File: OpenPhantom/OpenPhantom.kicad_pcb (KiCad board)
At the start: 2 copper layers, 175 x 175 mm, 94 parts, among them J1 Barrel_Jack, J2 Video, J3 Audio, Q1 BC548, Q2 BD136, Q3 BC557, Q4 BC548, SW1 POWER, SW2 RESET, U1 UM6116 VRAM, U10 74HC368, U11 74HC368, U2 UM6116 WRAM, U3 74HC04, U4 UA6547_CPU, U5 4013, U6 UA6548_PPU, U7 74HC139, U8 74LS373, U9 LM7805, Y1 21.453366 MHz

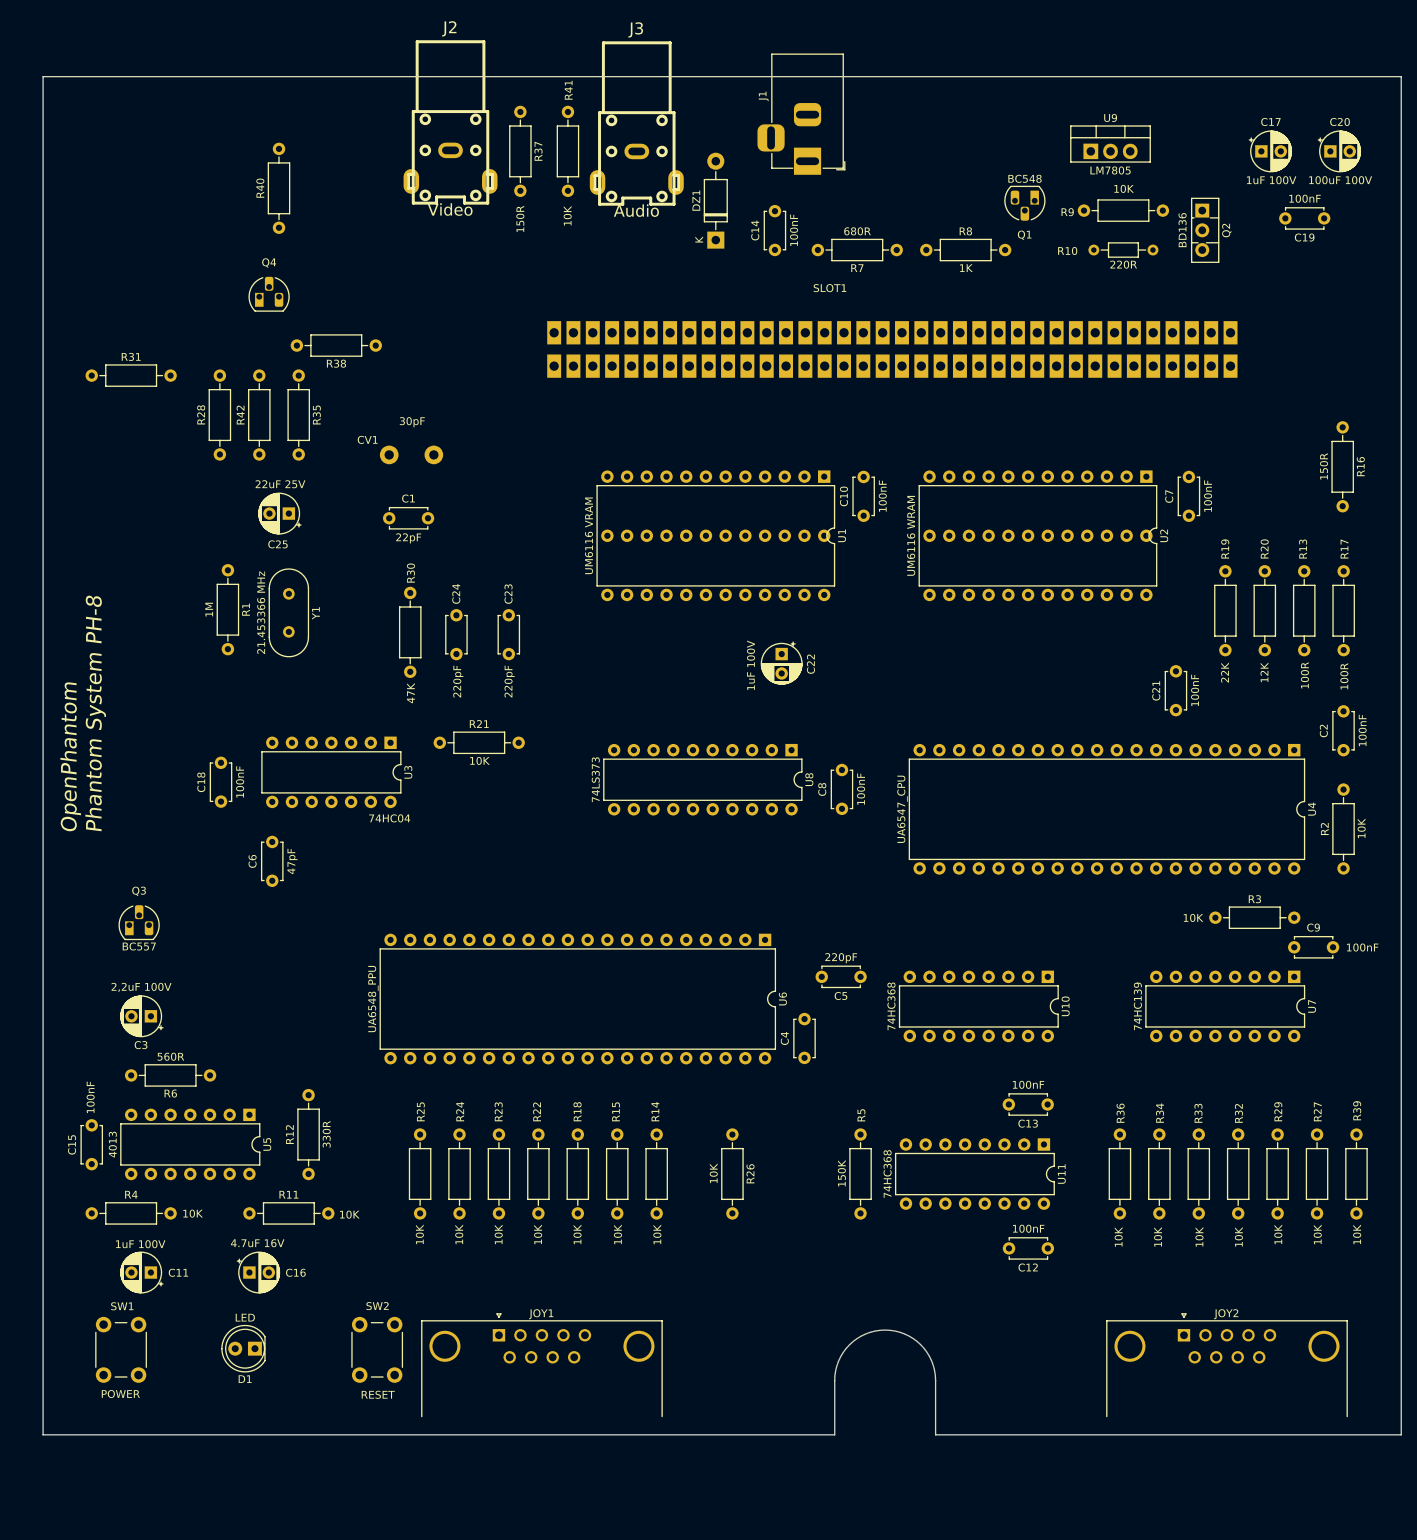
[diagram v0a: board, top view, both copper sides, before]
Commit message: PDF + PCB Routing + `Placement
Corrected component position. Added PCB Schematic PDF. Changed the logo. Moved the RCA connectors 2mm closer to the PCB edge.
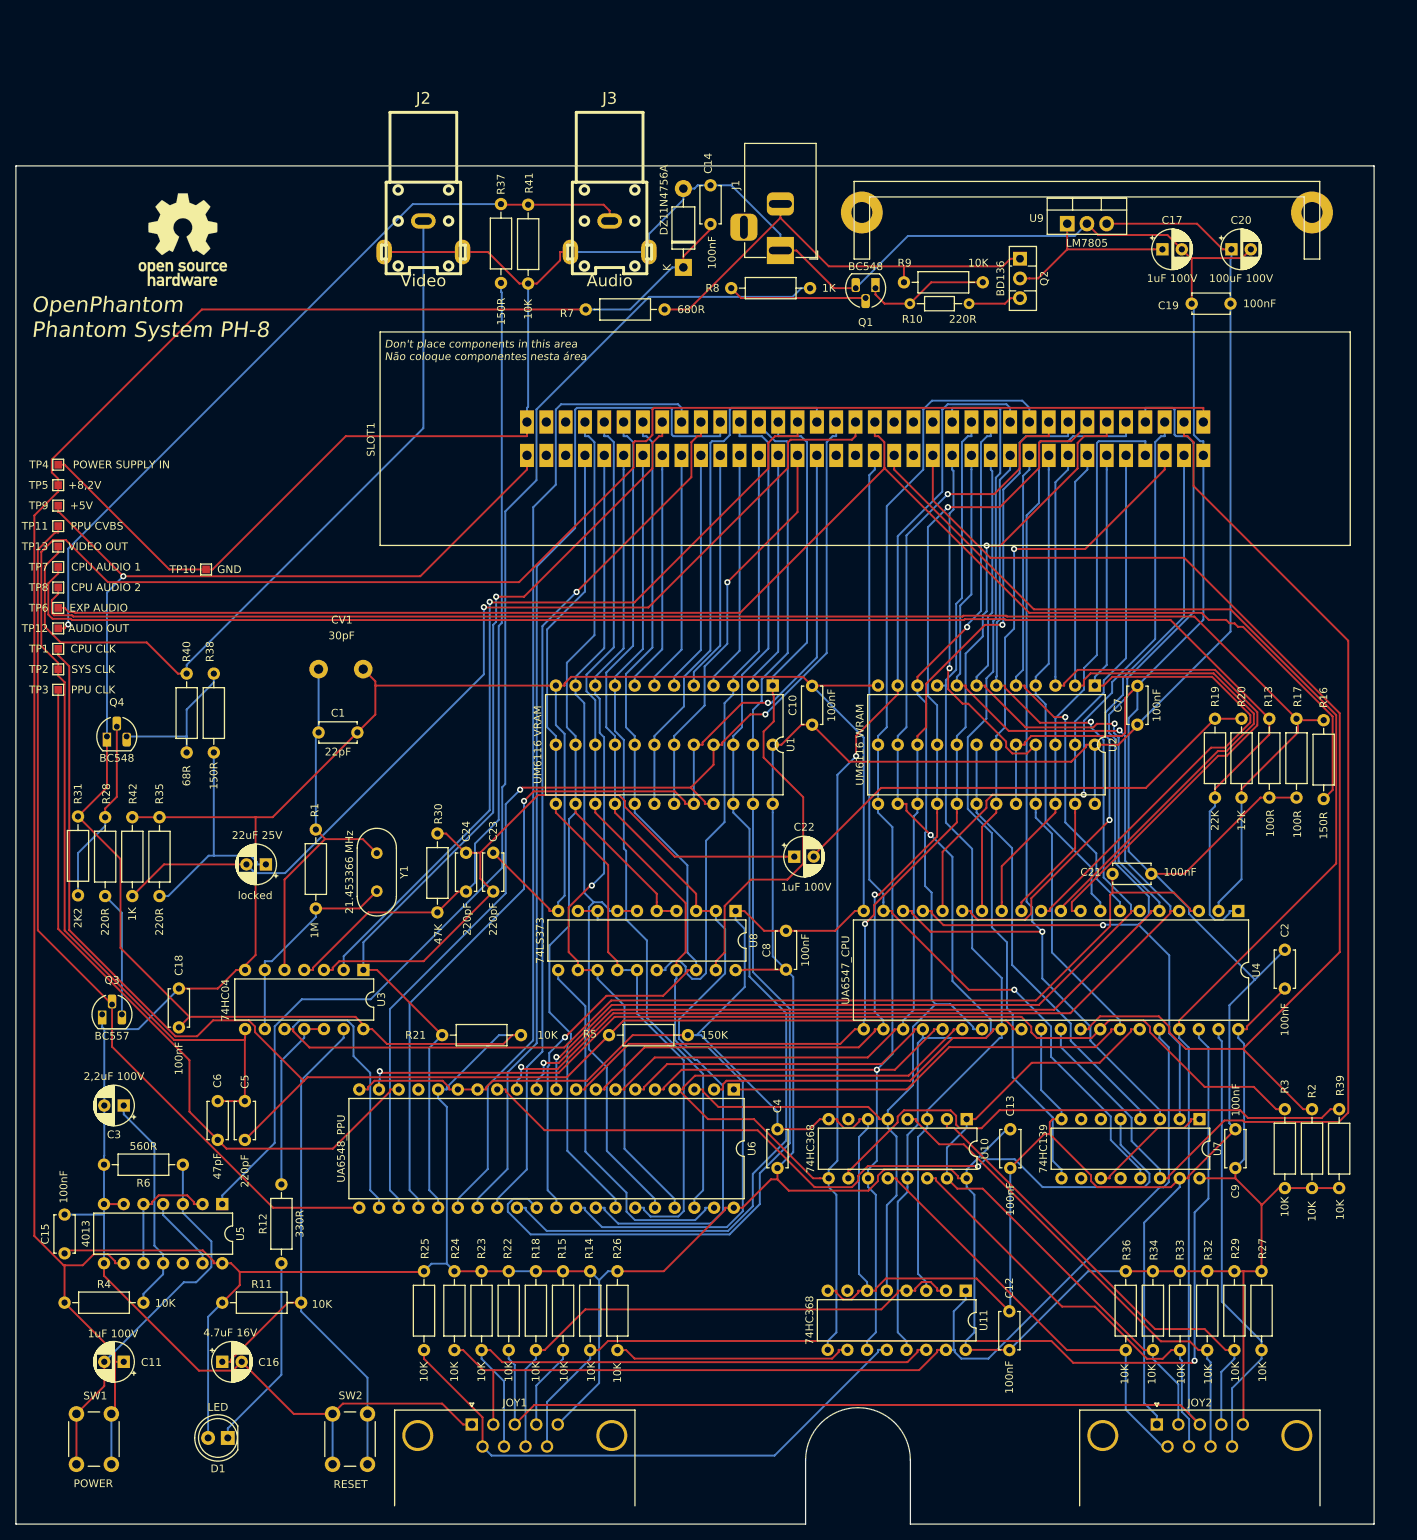
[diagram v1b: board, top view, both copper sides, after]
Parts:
- added PT1: MountingHole_2.7mm_M2.5_Pad, MountingHole:MountingHole_2.7mm_M2.5_Pad, F.Cu at (125.5, 32.0)
- added PT2: MountingHole_2.7mm_M2.5_Pad, MountingHole:MountingHole_2.7mm_M2.5_Pad, F.Cu at (183.5, 32.0)
- added REF**: OSHW-Logo_11.4x12mm_SilkScreen, Symbol:OSHW-Logo_11.4x12mm_SilkScreen, F.Cu at (38.0, 35.5)
- added TP1: CPU CLK, TestPoint:TestPoint_Pad_1.0x1.0mm, F.Cu at (21.9, 88.2)
- added TP10: GND, TestPoint:TestPoint_Pad_1.0x1.0mm, F.Cu at (41.0, 78.0)
- added TP11: PPU CVBS, TestPoint:TestPoint_Pad_1.0x1.0mm, F.Cu at (21.9, 72.4)
- added TP12: AUDIO OUT, TestPoint:TestPoint_Pad_1.0x1.0mm, F.Cu at (21.9, 85.6)
- added TP13: VIDEO OUT, TestPoint:TestPoint_Pad_1.0x1.0mm, F.Cu at (21.9, 75.0)
- added TP2: SYS CLK, TestPoint:TestPoint_Pad_1.0x1.0mm, F.Cu at (21.9, 90.9)
- added TP3: PPU CLK, TestPoint:TestPoint_Pad_1.0x1.0mm, F.Cu at (21.9, 93.5)
- added TP4: POWER SUPPLY IN, TestPoint:TestPoint_Pad_1.0x1.0mm, F.Cu at (21.9, 64.5)
- added TP5: +8,2V, TestPoint:TestPoint_Pad_1.0x1.0mm, F.Cu at (21.9, 67.1)
- added TP6: EXP AUDIO, TestPoint:TestPoint_Pad_1.0x1.0mm, F.Cu at (21.9, 83.0)
- added TP7: CPU AUDIO 1, TestPoint:TestPoint_Pad_1.0x1.0mm, F.Cu at (21.9, 77.7)
- added TP8: CPU AUDIO 2, TestPoint:TestPoint_Pad_1.0x1.0mm, F.Cu at (21.9, 80.3)
- added TP9: +5V, TestPoint:TestPoint_Pad_1.0x1.0mm, F.Cu at (21.9, 69.8)
- moved C5 82.1 mm to (46.0, 151.5), turned to 90 degrees
- moved R40 68.6 mm to (38.5, 101.6)
- moved Q4 60.0 mm to (28.2, 99.5)
- moved R35 59.7 mm to (35.0, 109.9)
- moved R42 59.2 mm to (31.5, 120.1)
- moved R28 58.8 mm to (28.0, 120.1)
- moved R31 56.8 mm to (24.5, 109.8), turned to -90 degrees
- moved R38 56.4 mm to (42.0, 101.6), turned to 90 degrees
- moved R16 48.0 mm to (185.0, 107.6), turned to 90 degrees
- moved locked 45.3 mm to (48.7, 116.0)
- moved R2 41.4 mm to (183.5, 157.7)
- moved R21 37.7 mm to (71.4, 138.0)
- moved R1 35.3 mm to (55.1, 111.5)
- moved Y1 35.3 mm to (63.0, 114.5)
- moved R3 34.9 mm to (180.0, 157.7), turned to 90 degrees
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- renumbered C25 to locked
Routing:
- net /GND: track 0.00 -> 1011.4 mm
- net /VCC: track 0.00 -> 751.6 mm, vias 0 -> 1
- net /EXP-1: track 0.00 -> 273.0 mm
- net /SYSTEM-CLK: track 0.00 -> 259.5 mm
- net /+8,2V: track 0.00 -> 244.3 mm
- net /CPU-D2: track 0.00 -> 203.8 mm, vias 0 -> 1
- net /EXP-6: track 0.00 -> 203.3 mm
- net /AUDIO-1: track 0.00 -> 202.7 mm
- net /AUDIO-2: track 0.00 -> 202.1 mm
- net /CPU-D4: track 0.00 -> 190.3 mm, vias 0 -> 2
- net /CPU-CLK: track 0.00 -> 184.3 mm
- net /CPU-D3: track 0.00 -> 183.4 mm, vias 0 -> 1
- net /CPU-A0: track 0.00 -> 177.7 mm, vias 0 -> 2
- net /CPU-A1: track 0.00 -> 168.9 mm, vias 0 -> 2
- net /RST: track 0.00 -> 167.7 mm
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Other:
- outline, holes or cut-outs redrawn
- board text added: "Don't place components in this area Não coloque componentes nesta área"

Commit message: Updated track and vias width
After some comments of other people that used the board, I remade the routing using a wider ground track. The other tracks were made wider too.
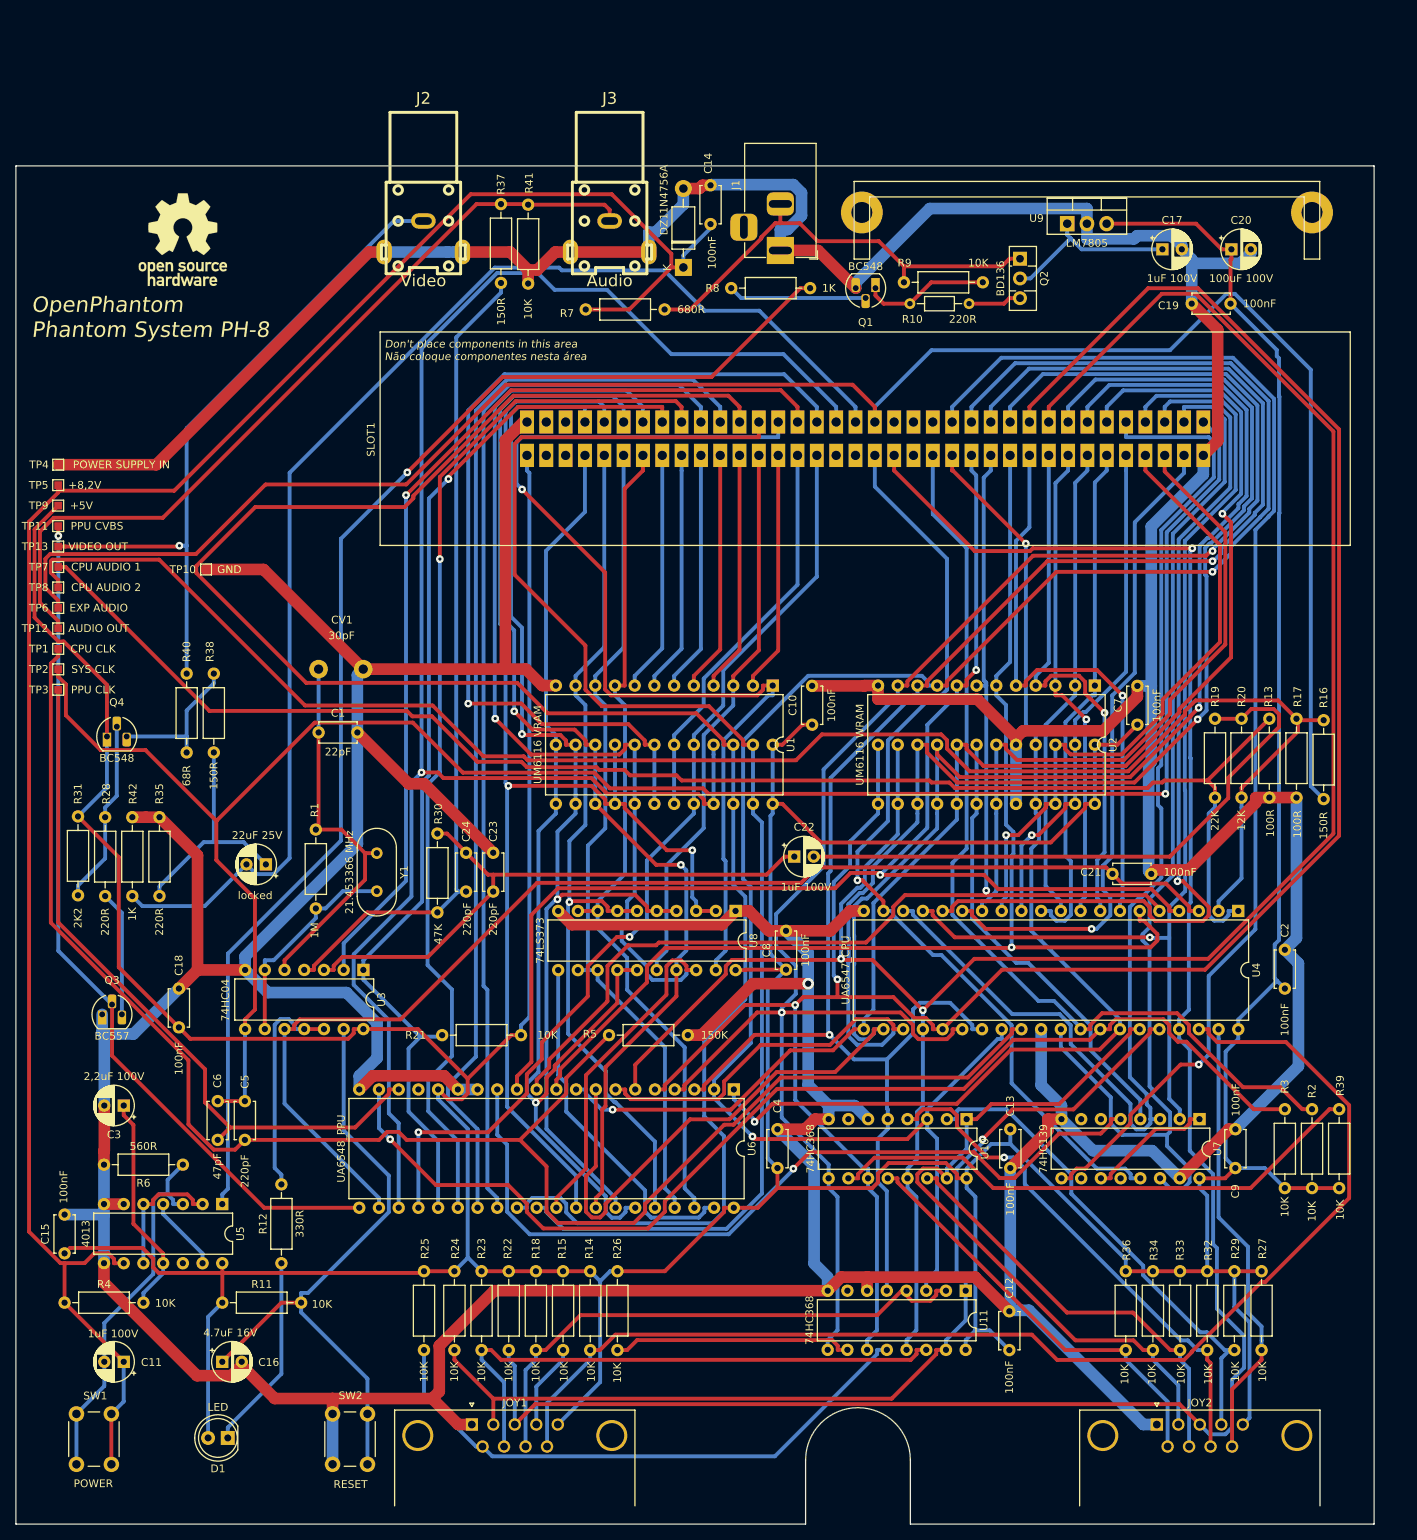
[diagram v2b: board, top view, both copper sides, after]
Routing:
- net /CPU-D3: track 183.4 -> 298.6 mm, vias 1 -> 2
- net /PPU-A9: track 143.9 -> 255.6 mm
- net /CPU-D4: track 190.3 -> 291.9 mm
- net /CPU-D0: track 163.5 -> 259.0 mm, vias 0 -> 2
- net /PPU-~{WE}: track 144.3 -> 230.5 mm, vias 2 -> 1
- net /CPU-D1: track 155.0 -> 238.2 mm, vias 1 -> 2
- net /CPU-D6: track 138.2 -> 218.9 mm, vias 2 -> 1
- net /CPU-D5: track 132.0 -> 208.1 mm
- net /VCC: track 751.6 -> 815.7 mm, vias 1 -> 0
- net /GND: track 1011.4 -> 1075.2 mm, vias 0 -> 1
- net /VRAM-~{CE}: track 68.8 -> 122.4 mm, vias 0 -> 1
- net /PPU-A7: track 85.8 -> 135.5 mm, vias 0 -> 1
- net /~{ROMSEL}: track 114.0 -> 162.8 mm, vias 0 -> 1
- net /CPU-D7: track 134.3 -> 181.6 mm
- net /EXP-6: track 203.3 -> 250.5 mm
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
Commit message: 74LS373 PPU AD Pins FIX
Fixed 74LS373 pins connected to the AD Pins from PPU (PPU D0 to D7)
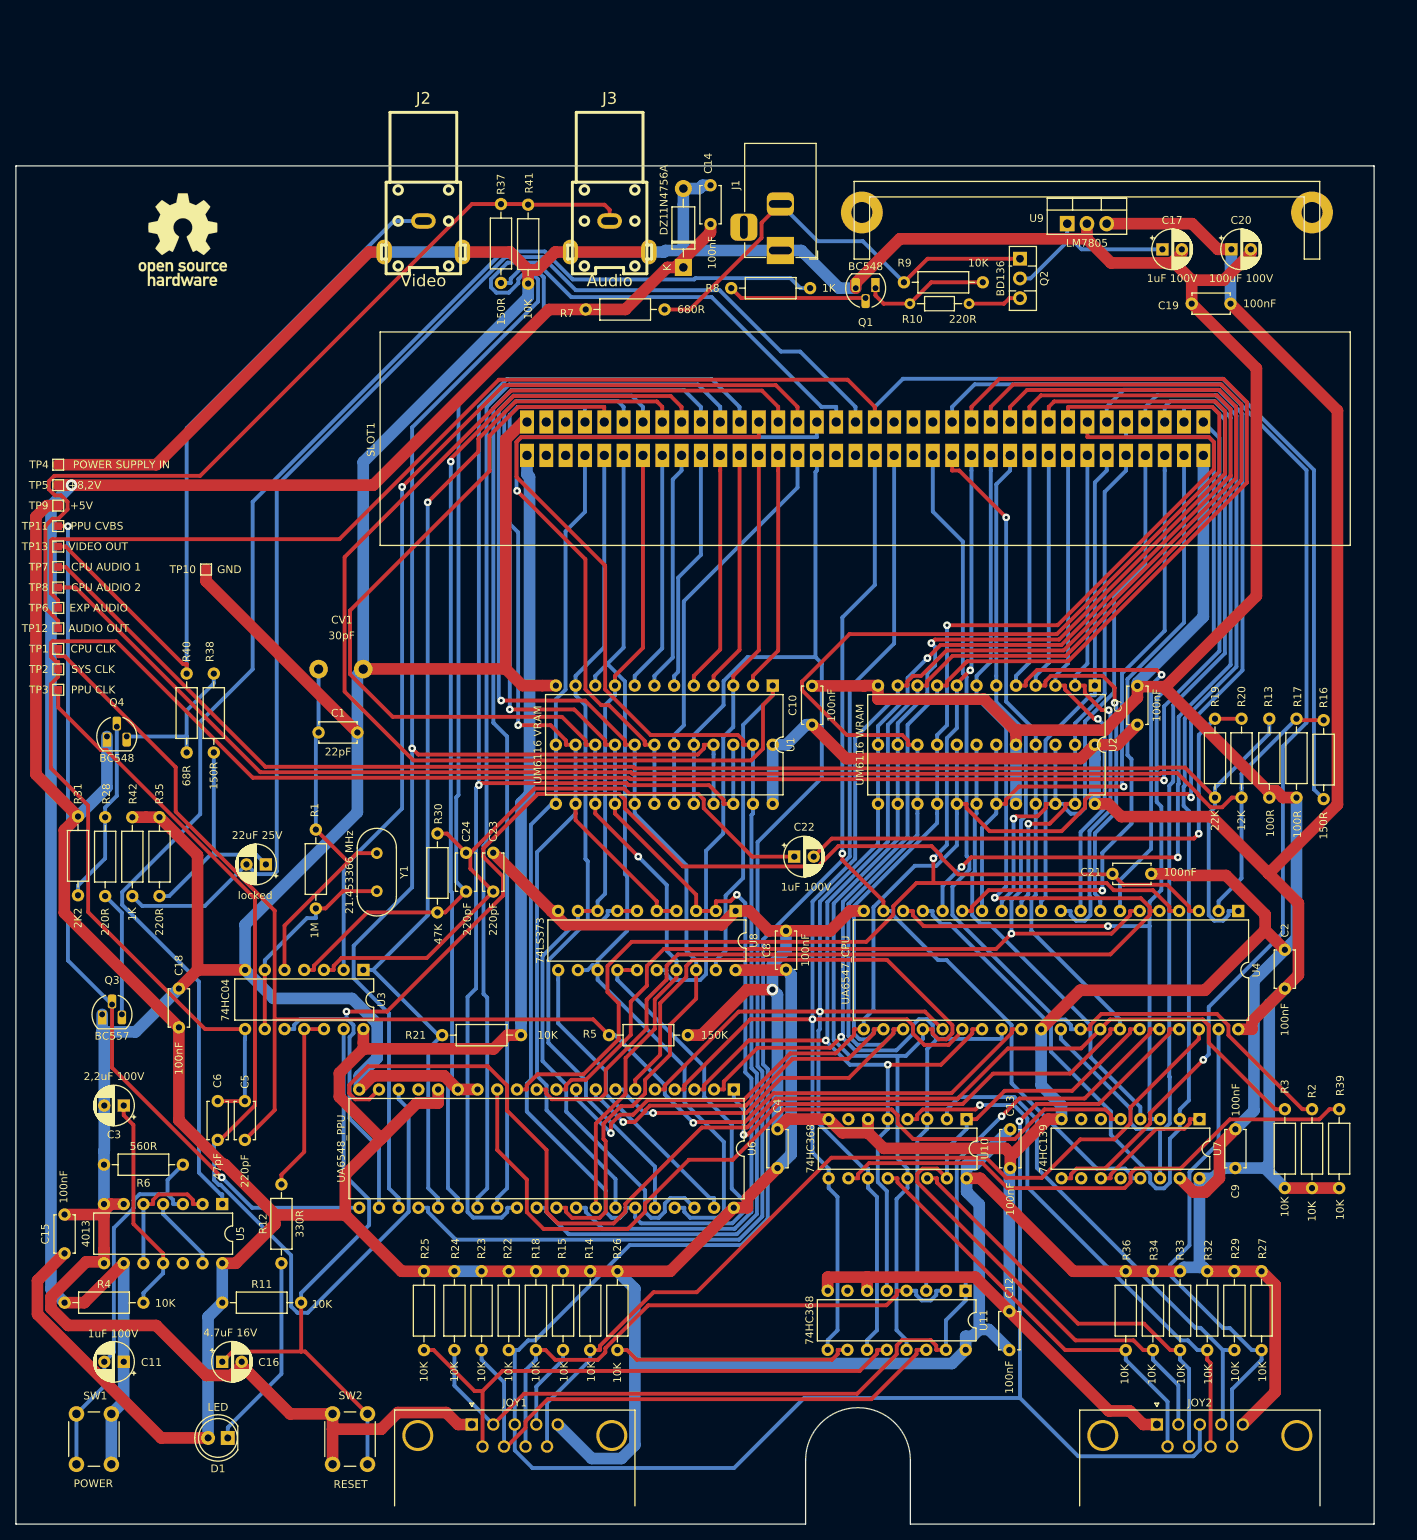
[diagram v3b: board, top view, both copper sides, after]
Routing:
- net /VCC: track 815.7 -> 899.1 mm
- net /CPU-D3: track 298.6 -> 228.0 mm
- net /PPU-A9: track 255.6 -> 192.3 mm, vias 0 -> 1
- net /PPU-A7: track 135.5 -> 191.5 mm, vias 1 -> 0
- net /PPU-~{RD}: track 124.4 -> 180.3 mm, vias 2 -> 0
- net /EXP-1: track 268.3 -> 320.4 mm
- net /CPU-D6: track 218.9 -> 172.1 mm, vias 1 -> 2
- net /OUT-1: track 159.1 -> 114.7 mm
- net /GND: track 1075.2 -> 1118.3 mm
- net /PPU-CLK: track 91.9 -> 134.2 mm
- net /CPU-D4: track 291.9 -> 254.0 mm, vias 2 -> 1
- net /PPU-D3: track 134.9 -> 166.9 mm, vias 1 -> 0
- net /CPU-CLK: track 216.4 -> 184.6 mm, vias 0 -> 1
- net /CPU-D0: track 259.0 -> 232.4 mm, vias 2 -> 1
- net /CPU-A13: track 143.6 -> 169.9 mm, vias 1 -> 0
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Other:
- board text removed: "Don't place components in this area Não coloque componentes nesta área"
- board text removed: "OpenPhantom Phantom System PH-8"
